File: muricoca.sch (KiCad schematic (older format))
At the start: 133 parts, among them J1 USB_B_Mini, SW1 Esc, SW10 9, SW11 0, SW12 -, SW13 =, SW14 Bksp, SW15 Tab, SW16 Q, SW17 W, SW18 E, SW19 R, SW2 1, SW20 T, SW21 Y, SW22 U, SW23 I, SW24 O, SW25 P, SW26 [, SW27 ], SW28 \\, SW29 Caps, SW3 2, SW30 A, SW31 S, SW32 D, SW33 F, SW34 G, SW35 H, SW36 J, SW37 K, SW38 L, SW39 ;, SW4 3, SW40 ', SW41 Enter, SW42 LShift, SW43 Z, SW44 X, SW45 C, SW46 V, SW47 B, SW48 N, SW49 M, SW5 4, SW50 ,, SW51 ., SW52 /, SW53 RShift, SW54 LCtrl, SW55 Alt, SW56 Space, SW57 Alt Gr, SW58 RCtrl, SW6 5, SW7 6, SW8 7, SW9 8, U1 ATmega32U4-AU, Y1 16Mhz

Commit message: chore: add keycaps' dimensions to the labels
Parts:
- SW14: value Bksp -> Bksp_200
- SW15: value Tab -> Tab_125
- SW28: value \\ -> \\_150
- SW29: value Caps -> Caps_175
- SW41: value Enter -> Enter_225
- SW42: value LShift -> LShift_225
- SW53: value RShift -> RShift_275
- SW54: value LCtrl -> LCtrl_150
- SW55: value Alt -> Alt_150
- SW56: value Space -> Space_700
- SW57: value Alt Gr -> Alt Gr_150
- SW58: value RCtrl -> RCtrl_150
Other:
- moved on the sheet: D56, SW56
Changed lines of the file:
@@
 P 8575 4025
 F 0 "SW15" H 8575 4050 50  0000 C CNN
-F 1 "Tab" H 8575 3925 79  0000 C CNN
+F 1 "Tab_125" H 8575 3925 59  0000 C CNN
 F 2 "acheron_MX:MX100" H 8575 4025 50  0001 C CNN
 F 3 "" H 8575 4025 50  0001 C CNN
@@
 P 18950 2950
 F 0 "SW14" H 18950 2975 50  0000 C CNN
-F 1 "Bksp" H 18950 2850 79  0000 C CNN
+F 1 "Bksp_200" H 18950 2850 59  0000 C CNN
 F 2 "acheron_MX:MX100" H 18950 2950 50  0001 C CNN
 F 3 "" H 18950 2950 50  0001 C CNN
@@
 P 18950 4025
 F 0 "SW28" H 18950 4050 50  0000 C CNN
-F 1 "\\" H 18950 3925 79  0000 C CNN
+F 1 "\\_150" H 18950 3925 59  0000 C CNN
 F 2 "acheron_MX:MX100" H 18950 4025 50  0001 C CNN
 F 3 "" H 18950 4025 50  0001 C CNN
@@
 P 18200 5100
 F 0 "SW41" H 18200 5125 50  0000 C CNN
-F 1 "Enter" H 18200 5000 79  0000 C CNN
+F 1 "Enter_225" H 18200 5000 59  0000 C CNN
 F 2 "acheron_MX:MX100" H 18200 5100 50  0001 C CNN
 F 3 "" H 18200 5100 50  0001 C CNN
@@
 P 8575 5100
 F 0 "SW29" H 8575 5125 50  0000 C CNN
-F 1 "Caps" H 8575 5000 79  0000 C CNN
+F 1 "Caps_175" H 8575 5000 59  0000 C CNN
 F 2 "acheron_MX:MX100" H 8575 5100 50  0001 C CNN
 F 3 "" H 8575 5100 50  0001 C CNN
@@
 	0    1    1    0
 $EndComp
-Wire Wire Line
-	13100 5100 13100 6175
 $Comp
 L acheronSymbols:MXSwitch SW48
@@
 P 17450 6175
 F 0 "SW53" H 17450 6200 50  0000 C CNN
-F 1 "RShift" H 17450 6075 79  0000 C CNN
+F 1 "RShift_275" H 17450 6075 59  0000 C CNN
 F 2 "acheron_MX:MX100" H 17450 6175 50  0001 C CNN
 F 3 "" H 17450 6175 50  0001 C CNN
@@
 P 8575 6175
 F 0 "SW42" H 8575 6200 50  0000 C CNN
-F 1 "LShift" H 8575 6075 79  0000 C CNN
+F 1 "LShift_225" H 8575 6075 59  0000 C CNN
 F 2 "acheron_MX:MX100" H 8575 6175 50  0001 C CNN
 F 3 "" H 8575 6175 50  0001 C CNN
@@
 $EndComp
 Wire Wire Line
-	13100 6175 13100 7250
-$Comp
-L acheronSymbols:MXSwitch SW56
-U 1 1 5F16233B
-P 13450 7250
-F 0 "SW56" H 13450 7275 50  0000 C CNN
-F 1 "Space" H 13450 7150 79  0000 C CNN
-F 2 "acheron_MX:MX100" H 13450 7250 50  0001 C CNN
-F 3 "" H 13450 7250 50  0001 C CNN
-	1    13450 7250
-	1    0    0    -1
-$EndComp
-$Comp
-L Device:D_Small D56
-U 1 1 5F162341
-P 13450 6800
-F 0 "D56" V 13404 6870 50  0000 L CNN
-F 1 "1N4148W" V 13495 6870 50  0000 L CNN
-F 2 "Diode_SMD:D_SOD-123" V 13450 6800 50  0001 C CNN
-F 3 "~" V 13450 6800 50  0001 C CNN
-	1    13450 6800
-	0    1    1    0
-$EndComp
-Wire Wire Line
 	17100 6175 17100 7250
 $Comp
@@
 P 17450 7250
 F 0 "SW57" H 17450 7275 50  0000 C CNN
-F 1 "Alt Gr" H 17450 7150 79  0000 C CNN
+F 1 "Alt Gr_150" H 17450 7150 59  0000 C CNN
 F 2 "acheron_MX:MX100" H 17450 7250 50  0001 C CNN
 F 3 "" H 17450 7250 50  0001 C CNN
@@
 Connection ~ 10325 6500
 Wire Wire Line
-	13450 6700 13450 6500
-Connection ~ 13450 6500
-Wire Wire Line
 	17450 6700 17450 6500
 $Comp
@@
 P 8575 7250
 F 0 "SW54" H 8575 7275 50  0000 C CNN
-F 1 "LCtrl" H 8575 7150 79  0000 C CNN
+F 1 "LCtrl_150" H 8575 7150 59  0000 C CNN
 F 2 "acheron_MX:MX100" H 8575 7250 50  0001 C CNN
 F 3 "" H 8575 7250 50  0001 C CNN
@@
 P 10325 7250
 F 0 "SW55" H 10325 7275 50  0000 C CNN
-F 1 "Alt" H 10325 7150 79  0000 C CNN
+F 1 "Alt_150" H 10325 7150 59  0000 C CNN
 F 2 "acheron_MX:MX100" H 10325 7250 50  0001 C CNN
 F 3 "" H 10325 7250 50  0001 C CNN
@@
 	1    0    0    -1
 $EndComp
-Wire Wire Line
-	10325 6500 13450 6500
-Wire Wire Line
-	13450 6500 17450 6500
 $Comp
 L acheronSymbols:MXSwitch SW58
@@
 P 18950 7250
 F 0 "SW58" H 18950 7275 50  0000 C CNN
-F 1 "RCtrl" H 18950 7150 79  0000 C CNN
+F 1 "RCtrl_150" H 18950 7150 59  0000 C CNN
 F 2 "acheron_MX:MX100" H 18950 7250 50  0001 C CNN
 F 3 "" H 18950 7250 50  0001 C CNN
@@
 	18950 6500 18950 6700
 Connection ~ 17450 6500
+Wire Wire Line
+	13100 5100 13100 6175
+Wire Wire Line
+	13875 6700 13875 6500
+$Comp
+L Device:D_Small D56
+U 1 1 5F162341
+P 13875 6800
+F 0 "D56" V 13829 6870 50  0000 L CNN
+F 1 "1N4148W" V 13920 6870 50  0000 L CNN
+F 2 "Diode_SMD:D_SOD-123" V 13875 6800 50  0001 C CNN
+F 3 "~" V 13875 6800 50  0001 C CNN
+	1    13875 6800
+	0    1    1    0
+$EndComp
+$Comp
+L acheronSymbols:MXSwitch SW56
+U 1 1 5F16233B
+P 13875 7250
+F 0 "SW56" H 13875 7275 50  0000 C CNN
+F 1 "Space_700" H 13875 7150 59  0000 C CNN
+F 2 "acheron_MX:MX100" H 13875 7250 50  0001 C CNN
+F 3 "" H 13875 7250 50  0001 C CNN
+	1    13875 7250
+	1    0    0    -1
+$EndComp
+Wire Wire Line
+	13100 6175 13100 7250
+Connection ~ 13875 6500
+Wire Wire Line
+	13875 6500 17450 6500
+Wire Wire Line
+	10325 6500 13875 6500
+Wire Wire Line
+	13100 7250 13525 7250
 $EndSCHEMATC

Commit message: chore: assign the correct footprints for the keys bigger than 1u
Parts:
- SW14: footprint acheron_MX:MX100 -> acheron_MX:MX200
- SW15: footprint acheron_MX:MX100 -> acheron_MX:MX125
- SW28, SW54, SW55, SW57, SW58: footprint acheron_MX:MX100 -> acheron_MX:MX150
- SW29: footprint acheron_MX:MX100 -> acheron_MX:MX175
- SW41, SW42: footprint acheron_MX:MX100 -> acheron_MX:MX225
- SW53: footprint acheron_MX:MX100 -> acheron_MX:MX275
- SW56: footprint acheron_MX:MX100 -> acheron_MX:MX700
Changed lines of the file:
@@
 F 0 "SW15" H 8575 4050 50  0000 C CNN
 F 1 "Tab_125" H 8575 3925 59  0000 C CNN
-F 2 "acheron_MX:MX100" H 8575 4025 50  0001 C CNN
+F 2 "acheron_MX:MX125" H 8575 4025 50  0001 C CNN
 F 3 "" H 8575 4025 50  0001 C CNN
 	1    8575 4025
@@
 F 0 "SW14" H 18950 2975 50  0000 C CNN
 F 1 "Bksp_200" H 18950 2850 59  0000 C CNN
-F 2 "acheron_MX:MX100" H 18950 2950 50  0001 C CNN
+F 2 "acheron_MX:MX200" H 18950 2950 50  0001 C CNN
 F 3 "" H 18950 2950 50  0001 C CNN
 	1    18950 2950
@@
 F 0 "SW28" H 18950 4050 50  0000 C CNN
 F 1 "\\_150" H 18950 3925 59  0000 C CNN
-F 2 "acheron_MX:MX100" H 18950 4025 50  0001 C CNN
+F 2 "acheron_MX:MX150" H 18950 4025 50  0001 C CNN
 F 3 "" H 18950 4025 50  0001 C CNN
 	1    18950 4025
@@
 F 0 "SW41" H 18200 5125 50  0000 C CNN
 F 1 "Enter_225" H 18200 5000 59  0000 C CNN
-F 2 "acheron_MX:MX100" H 18200 5100 50  0001 C CNN
+F 2 "acheron_MX:MX225" H 18200 5100 50  0001 C CNN
 F 3 "" H 18200 5100 50  0001 C CNN
 	1    18200 5100
@@
 F 0 "SW29" H 8575 5125 50  0000 C CNN
 F 1 "Caps_175" H 8575 5000 59  0000 C CNN
-F 2 "acheron_MX:MX100" H 8575 5100 50  0001 C CNN
+F 2 "acheron_MX:MX175" H 8575 5100 50  0001 C CNN
 F 3 "" H 8575 5100 50  0001 C CNN
 	1    8575 5100
@@
 F 0 "SW53" H 17450 6200 50  0000 C CNN
 F 1 "RShift_275" H 17450 6075 59  0000 C CNN
-F 2 "acheron_MX:MX100" H 17450 6175 50  0001 C CNN
+F 2 "acheron_MX:MX275" H 17450 6175 50  0001 C CNN
 F 3 "" H 17450 6175 50  0001 C CNN
 	1    17450 6175
@@
 F 0 "SW42" H 8575 6200 50  0000 C CNN
 F 1 "LShift_225" H 8575 6075 59  0000 C CNN
-F 2 "acheron_MX:MX100" H 8575 6175 50  0001 C CNN
+F 2 "acheron_MX:MX225" H 8575 6175 50  0001 C CNN
 F 3 "" H 8575 6175 50  0001 C CNN
 	1    8575 6175
@@
 F 0 "SW57" H 17450 7275 50  0000 C CNN
 F 1 "Alt Gr_150" H 17450 7150 59  0000 C CNN
-F 2 "acheron_MX:MX100" H 17450 7250 50  0001 C CNN
+F 2 "acheron_MX:MX150" H 17450 7250 50  0001 C CNN
 F 3 "" H 17450 7250 50  0001 C CNN
 	1    17450 7250
@@
 F 0 "SW54" H 8575 7275 50  0000 C CNN
 F 1 "LCtrl_150" H 8575 7150 59  0000 C CNN
-F 2 "acheron_MX:MX100" H 8575 7250 50  0001 C CNN
+F 2 "acheron_MX:MX150" H 8575 7250 50  0001 C CNN
 F 3 "" H 8575 7250 50  0001 C CNN
 	1    8575 7250
@@
 F 0 "SW55" H 10325 7275 50  0000 C CNN
 F 1 "Alt_150" H 10325 7150 59  0000 C CNN
-F 2 "acheron_MX:MX100" H 10325 7250 50  0001 C CNN
+F 2 "acheron_MX:MX150" H 10325 7250 50  0001 C CNN
 F 3 "" H 10325 7250 50  0001 C CNN
 	1    10325 7250
@@
 F 0 "SW58" H 18950 7275 50  0000 C CNN
 F 1 "RCtrl_150" H 18950 7150 59  0000 C CNN
-F 2 "acheron_MX:MX100" H 18950 7250 50  0001 C CNN
+F 2 "acheron_MX:MX150" H 18950 7250 50  0001 C CNN
 F 3 "" H 18950 7250 50  0001 C CNN
 	1    18950 7250
@@
 F 0 "SW56" H 13875 7275 50  0000 C CNN
 F 1 "Space_700" H 13875 7150 59  0000 C CNN
-F 2 "acheron_MX:MX100" H 13875 7250 50  0001 C CNN
+F 2 "acheron_MX:MX700" H 13875 7250 50  0001 C CNN
 F 3 "" H 13875 7250 50  0001 C CNN
 	1    13875 7250

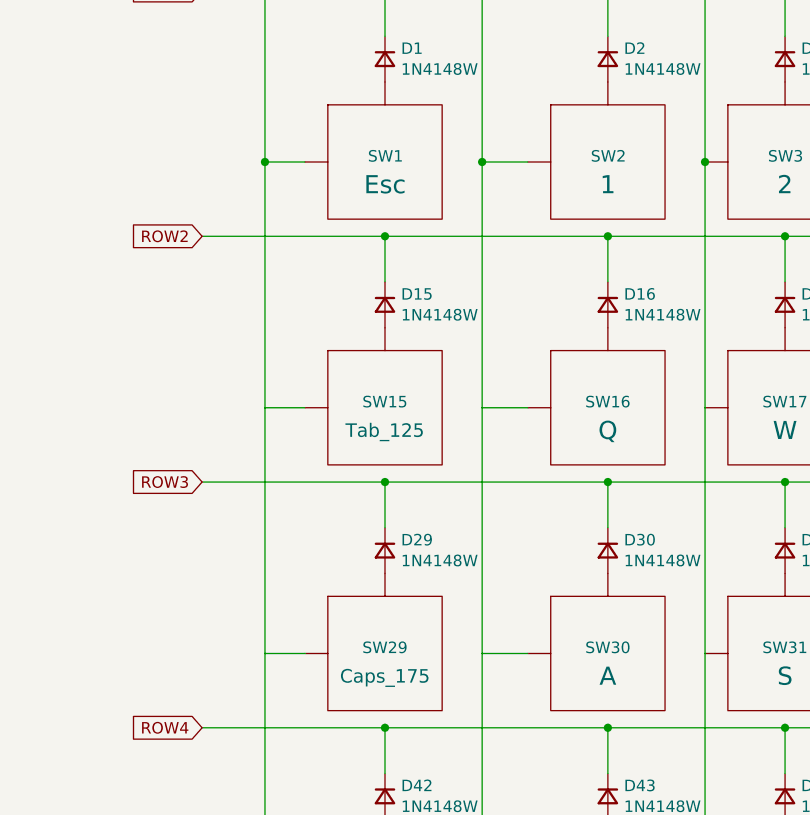
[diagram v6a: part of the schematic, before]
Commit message: feat: align the switches on the PCB
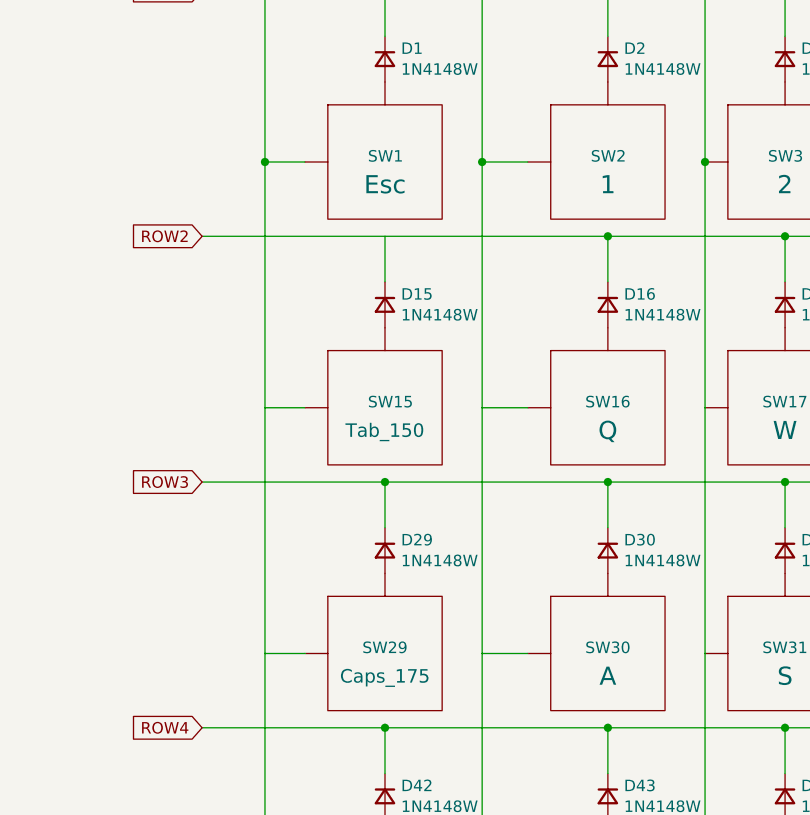
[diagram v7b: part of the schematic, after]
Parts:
- SW15: value Tab_125 -> Tab_150; footprint acheron_MX:MX125 -> acheron_MX:MX150
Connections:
- net COL1: no longer SW15.1 (Col)
- net ROW2: no longer D15.1 (K)
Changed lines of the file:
@@
-$EndComp
-$Comp
-L acheronSymbols:MXSwitch SW15
-U 1 1 5EE3DBE1
-P 8575 4025
-F 0 "SW15" H 8575 4050 50  0000 C CNN
-F 1 "Tab_125" H 8575 3925 59  0000 C CNN
-F 2 "acheron_MX:MX125" H 8575 4025 50  0001 C CNN
-F 3 "" H 8575 4025 50  0001 C CNN
-	1    8575 4025
-	1    0    0    -1
-$EndComp
-$Comp
-L Device:D_Small D15
-U 1 1 5EE3DBE7
-P 8575 3575
-F 0 "D15" V 8529 3645 50  0000 L CNN
-F 1 "1N4148W" V 8620 3645 50  0000 L CNN
-F 2 "Diode_SMD:D_SOD-123" V 8575 3575 50  0001 C CNN
-F 3 "~" V 8575 3575 50  0001 C CNN
-	1    8575 3575
-	0    1    1    0
 $EndComp
 $Comp
@@
 	9550 3475 9550 3275
 Wire Wire Line
-	8575 3475 8575 3275
-Connection ~ 8575 3275
-Wire Wire Line
-	8575 3275 7775 3275
-Wire Wire Line
-	8225 4025 8050 4025
-Wire Wire Line
-	8050 4025 8050 2950
-Wire Wire Line
 	8050 2950 8225 2950
 Connection ~ 8050 2950
@@
 Wire Wire Line
 	9200 2950 9000 2950
-Wire Wire Line
-	8575 3275 9550 3275
 Connection ~ 8575 2200
 Text GLabel 7775 2200 0    50   Input ~ 0
@@
 Wire Wire Line
 	8225 5100 8050 5100
-Wire Wire Line
-	8050 5100 8050 4025
 Text GLabel 7775 4350 0    50   Input ~ 0
 ROW3
@@
 Wire Wire Line
 	13100 7250 13525 7250
+Wire Wire Line
+	7775 3275 9550 3275
+Wire Wire Line
+	8050 2950 8050 5100
+$Comp
+L Device:D_Small D15
+U 1 1 5EE55104
+P 8575 3575
+F 0 "D15" V 8529 3645 50  0000 L CNN
+F 1 "1N4148W" V 8620 3645 50  0000 L CNN
+F 2 "Diode_SMD:D_SOD-123" V 8575 3575 50  0001 C CNN
+F 3 "~" V 8575 3575 50  0001 C CNN
+	1    8575 3575
+	0    1    1    0
+$EndComp
+Wire Wire Line
+	8575 3475 8575 3275
+Wire Wire Line
+	8050 4025 8225 4025
+$Comp
+L acheronSymbols:MXSwitch SW15
+U 1 1 5EE5510C
+P 8575 4025
+F 0 "SW15" H 8500 4050 50  0000 L CNN
+F 1 "Tab_150" H 8575 3925 59  0000 C CNN
+F 2 "acheron_MX:MX150" H 8575 4025 50  0001 C CNN
+F 3 "" H 8575 4025 50  0001 C CNN
+	1    8575 4025
+	1    0    0    -1
+$EndComp
 $EndSCHEMATC
